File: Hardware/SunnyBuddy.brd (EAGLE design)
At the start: 43.2 x 47 mm, 29 parts, among them J1 5.5x2.1mm Barrel, J3 POWER_JACKPTH, J5 M02PTH, J6 M023.5MM, J7 M023.5MM, J8 M023.5MM, U1 LT3652

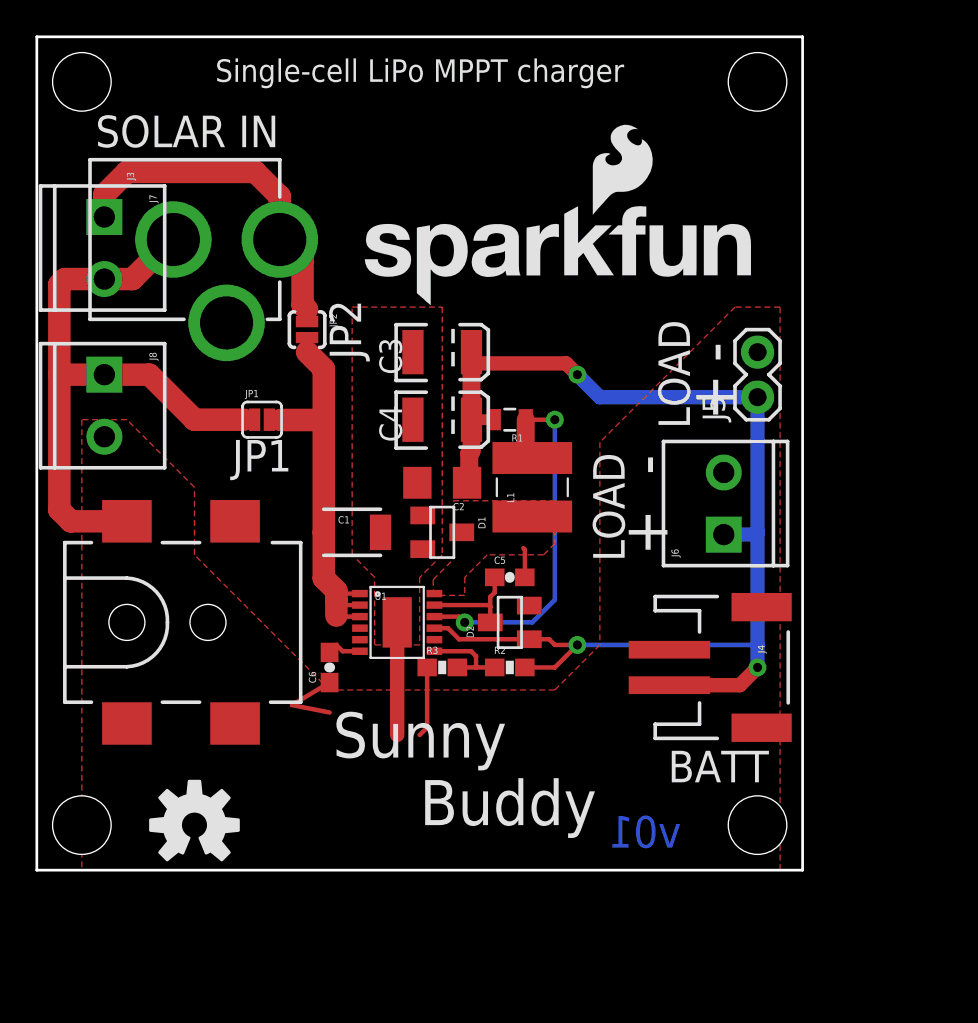
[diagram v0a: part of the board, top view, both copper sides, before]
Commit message: New inductor, better fb, add CHG and FLT
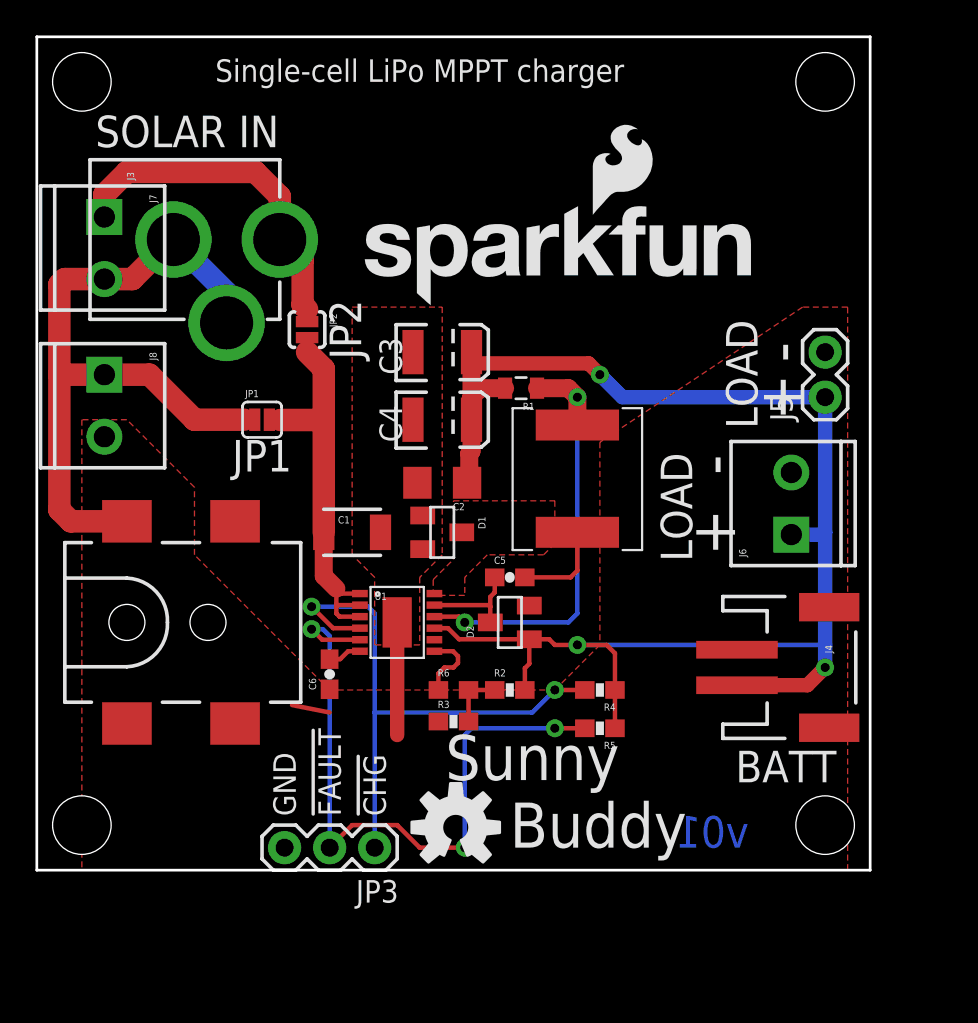
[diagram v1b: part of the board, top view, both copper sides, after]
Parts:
- added JP3: (no value), SparkFun-Connectors:1X03
- added R4, R5: 10K, SparkFun-Resistors:0603-RES
- added R6: 0, SparkFun-Resistors:0603
- L1: value 56uH -> 68uH; device SparkFun-Passives:SDR0403 -> SparkFun-Passives:CR75
- moved LOGO2 14.7 mm to (23.6, 2.41)
- moved J4 3.81 mm to (43.2, 11.4)
- moved J5 3.81 mm to (44.5, 26.7)
- moved J6 3.81 mm to (42.5, 18.9)
- moved STANDOFF3 3.81 mm to (44.5, 44.5)
- moved STANDOFF4 3.81 mm to (44.5, 2.54)
- moved L1 3.59 mm to (30.5, 19.1)
- moved R3 3.11 mm to (23.5, 8.38)
- moved R1 1.89 mm to (27.3, 27.2)
- moved R2 1.27 mm to (26.7, 10.2)
- moved C6 0.38 mm to (16.5, 11.0)
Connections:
- new net N$3: R6.1, U1.7
- net !CHRG: now also JP3.1, R4.2
- net !FAULT: now also JP3.2, R5.2
- net FB: now also R6.2; no longer U1.7
- net GND: now also J1.GND, JP3.3
- net N$8: now also J3.GNDBREAK
- net V_BATT: now also R4.1, R5.1
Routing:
- net !FAULT: track 0.00 -> 38.0 mm, vias 0 -> 3
- net !CHRG: track 0.00 -> 32.5 mm, vias 0 -> 2
- net V_BATT: track 70.6 -> 85.1 mm
- net GND: track 15.0 -> 8.51 mm
- net N$8: track 36.3 -> 42.3 mm
- net N$3: track 0.00 -> 4.10 mm
- net SW: track 1.69 -> 5.28 mm
- net SENSE: track 21.6 -> 24.7 mm
- net FB: track 5.21 -> 3.25 mm
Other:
- board size 43.2 x 47 mm -> 47 x 47 mm
- board text added: "!CHG"
- board text added: "!FAULT"
- board text added: "GND"

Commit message: Change version numbers
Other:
- board text added: "v02"
- board text removed: "v01"
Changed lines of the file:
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@@
 <text x="18.288" y="30.48" size="1.778" layer="21" font="vector" ratio="15" rot="R90" align="bottom-center">JP2</text>
 <text x="82.55" y="-26.67" size="1.778" layer="25" font="vector" ratio="15" align="bottom-center">M. Hord</text>
-<text x="38.1" y="1.27" size="1.778" layer="16" font="vector" ratio="15" rot="MR0" align="bottom-center">v01</text>
+<text x="38.1" y="1.27" size="1.778" layer="16" font="vector" ratio="15" rot="MR0" align="bottom-center">v02</text>
 <text x="3.302" y="40.767" size="1.778" layer="21" font="vector" ratio="15">SOLAR IN</text>
 <text x="40.64" y="24.892" size="1.778" layer="21" font="vector" ratio="15" rot="R90">LOAD</text>

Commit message: Release to reds, chg v#, move 1 via, add pol silk
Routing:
- net !FAULT: track 38.0 -> 36.1 mm
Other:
- board text added: "v10"
- board text removed: "v02"
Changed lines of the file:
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@@
 <text x="12.7" y="22.479" size="1.778" layer="21" font="vector" ratio="15" align="bottom-center">JP1</text>
 <text x="18.288" y="30.48" size="1.778" layer="21" font="vector" ratio="15" rot="R90" align="bottom-center">JP2</text>
-<text x="82.55" y="-26.67" size="1.778" layer="25" font="vector" ratio="15" align="bottom-center">M. Hord</text>
-<text x="38.1" y="1.27" size="1.778" layer="16" font="vector" ratio="15" rot="MR0" align="bottom-center">v02</text>
+<text x="82.55" y="-26.67" size="1.778" layer="51" font="vector" ratio="15" align="bottom-center">M. Hord</text>
+<text x="38.1" y="1.27" size="1.778" layer="16" font="vector" ratio="15" rot="MR0" align="bottom-center">v10</text>
 <text x="3.302" y="40.767" size="1.778" layer="21" font="vector" ratio="15">SOLAR IN</text>
 <text x="40.64" y="24.892" size="1.778" layer="21" font="vector" ratio="15" rot="R90">LOAD</text>
 <text x="36.957" y="17.399" size="1.778" layer="21" font="vector" ratio="15" rot="R90">LOAD</text>
 <text x="45.085" y="6.731" size="1.778" layer="21" font="vector" ratio="15" rot="R180">BATT</text>
-<text x="21.59" y="44.45" size="1.27" layer="21" font="vector" ratio="15" rot="R180" align="top-center">Single-cell LiPo MPPT charger</text>
+<text x="23.495" y="44.45" size="1.27" layer="21" font="vector" ratio="15" rot="R180" align="top-center">Single-cell LiPo MPPT charger</text>
 <text x="19.05" y="3.048" size="1.27" layer="21" font="vector" ratio="15" rot="R90" align="center-left">!CHG</text>
 <text x="16.51" y="3.048" size="1.27" layer="21" font="vector" ratio="15" rot="R90" align="center-left">!FAULT</text>
 <text x="13.97" y="3.048" size="1.27" layer="21" font="vector" ratio="15" rot="R90" align="center-left">GND</text>
+<text x="9.652" y="28.194" size="2.54" layer="21" font="vector" ratio="15" rot="R90" align="bottom-center">+</text>
+<text x="9.652" y="24.892" size="2.54" layer="21" font="vector" ratio="15" rot="R90" align="bottom-center">-</text>
+<text x="9.144" y="39.37" size="2.54" layer="21" font="vector" ratio="15" rot="R90" align="bottom-center">+</text>
+<text x="9.144" y="32.512" size="2.54" layer="21" font="vector" ratio="15" rot="R90" align="bottom-center">-</text>
 </plain>
 <attributes>
@@
 <wire x1="16.129" y1="13.589" x2="16.51" y2="13.208" width="0.254" layer="16"/>
 <wire x1="16.51" y1="13.208" x2="16.51" y2="1.27" width="0.254" layer="16"/>
-<wire x1="24.13" y1="7.62" x2="24.13" y2="1.27" width="0.254" layer="16"/>
-<via x="24.13" y="1.27" extent="1-16" drill="0.508"/>
-<wire x1="24.13" y1="1.27" x2="21.59" y2="1.27" width="0.254" layer="1"/>
-<wire x1="21.59" y1="1.27" x2="20.32" y2="2.54" width="0.254" layer="1"/>
+<wire x1="23.622" y1="7.112" x2="23.622" y2="2.413" width="0.254" layer="16"/>
+<via x="23.622" y="2.413" extent="1-16" drill="0.508"/>
+<wire x1="23.622" y1="2.413" x2="20.447" y2="2.413" width="0.254" layer="1"/>
+<wire x1="20.447" y1="2.413" x2="20.32" y2="2.54" width="0.254" layer="1"/>
 <wire x1="20.32" y1="2.54" x2="17.78" y2="2.54" width="0.254" layer="1"/>
 <wire x1="17.78" y1="2.54" x2="16.51" y2="1.27" width="0.254" layer="1"/>
 <wire x1="30.9" y1="8.001" x2="29.21" y2="8.001" width="0.254" layer="1"/>
 <via x="29.21" y="8.001" extent="1-16" drill="0.508"/>
-<wire x1="24.13" y1="7.62" x2="24.511" y2="8.001" width="0.254" layer="16"/>
+<wire x1="23.622" y1="7.112" x2="24.511" y2="8.001" width="0.254" layer="16"/>
 <wire x1="24.511" y1="8.001" x2="29.21" y2="8.001" width="0.254" layer="16"/>
 </signal>
